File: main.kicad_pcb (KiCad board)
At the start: 2 copper layers, 19 parts, among them SW1 Switch, SW2 Switch, SW3 Switch, SW4 Switch, SW5 Switch, SW6 Switch, SW7 Switch, SW8 Switch, SW9 Switch

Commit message: finished PCB
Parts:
- moved A1 64.2 mm to (138.5, 45.0), turned to -90 degrees
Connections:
- net col 3 renamed Net-(A1-GPIO6)
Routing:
- net Net-(A1-GPIO6): track 113.5 -> 394.6 mm
- net col 1: track 54.9 -> 191.1 mm
- net row 2: track 142.4 -> 102.9 mm
- net Net-(A1-GPIO0): track 104.0 -> 75.8 mm
- net row 3: track 104.3 -> 128.1 mm
- net col2: track 56.3 -> 69.7 mm
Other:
- board outline added: 70.5 x 86 mm

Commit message: made shell for pcb
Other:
- board size 70.5 x 86 mm -> 80 x 88.5 mm
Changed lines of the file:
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@@
 	)
 	(gr_rect
-		(start 108 28)
-		(end 178.5 114)
+		(start 108 27)
+		(end 188 115.5)
 		(stroke
 			(width 0.05)
@@
 		(fill no)
 		(layer "Edge.Cuts")
+	)
+	(dimension
+		(type orthogonal)
+		(layer "Edge.Cuts")
+		(pts
+			(xy 108.5 28) (xy 108.5 114)
+		)
+		(height -25)
+		(orientation 1)
+		(format
+			(prefix "")
+			(suffix "")
+			(units 3)
+			(units_format 0)
+			(precision 4)
+			(suppress_zeroes yes)
+		)
+		(style
+			(thickness 0.05)
+			(arrow_length 1.27)
+			(text_position_mode 0)
+			(arrow_direction outward)
+			(extension_height 0.58642)
+			(extension_offset 0.5)
+			(keep_text_aligned yes)
+		)
+		(gr_text "86"
+			(at 82.35 71 90)
+			(layer "Edge.Cuts")
+			(effects
+				(font
+					(size 1 1)
+					(thickness 0.15)
+				)
+			)
+		)
+	)
+	(dimension
+		(type orthogonal)
+		(layer "Edge.Cuts")
+		(pts
+			(xy 178.5 114) (xy 109 114)
+		)
+		(height 21)
+		(orientation 0)
+		(format
+			(prefix "")
+			(suffix "")
+			(units 3)
+			(units_format 0)
+			(precision 4)
+			(suppress_zeroes yes)
+		)
+		(style
+			(thickness 0.05)
+			(arrow_length 1.27)
+			(text_position_mode 0)
+			(arrow_direction outward)
+			(extension_height 0.58642)
+			(extension_offset 0.5)
+			(keep_text_aligned yes)
+		)
+		(gr_text "69.5"
+			(at 143.75 133.85 0)
+			(layer "Edge.Cuts")
+			(effects
+				(font
+					(size 1 1)
+					(thickness 0.15)
+				)
+			)
+		)
 	)
 	(segment
@@
 			)
 		)
+	)
+	(zone
+		(net 0)
+		(net_name "")
+		(layer "User.1")
+		(hatch edge 0.5)
+		(connect_pads
+			(clearance 0)
+		)
+		(min_thickness 0.25)
+		(filled_areas_thickness no)
+		(keepout
+			(tracks not_allowed)
+			(vias not_allowed)
+			(pads not_allowed)
+			(copperpour allowed)
+			(footprints allowed)
+		)
+		(placement
+			(enabled no)
+			(sheetname "/")
+		)
+		(fill
+			(thermal_gap 0.5)
+			(thermal_bridge_width 0.5)
+		)
+		(polygon
+			(pts
+				(xy 192 24) (xy 192 118) (xy 105 118) (xy 104.5 117.5) (xy 104.5 24.5) (xy 105 24)
+			)
+		)

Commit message: fixed pcb
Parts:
- moved A1 2.89 mm to (138.5, 42.1), turned to 90 degrees
- moved D7 0.42 mm to (168.5, 67.5)
- moved D1 0.23 mm to (130.5, 67.5)
- moved D4 0.23 mm to (149.5, 67.5)
- moved SW7 0.10 mm to (160.0, 65.0)
- moved D3 0.08 mm to (130.5, 105.5)
- moved D6 0.08 mm to (149.5, 105.5)
- moved D9 0.08 mm to (168.5, 105.5)
- moved SW2 0.08 mm to (121.9, 84.1)
- moved SW5 0.08 mm to (140.9, 84.1)
- moved SW8 0.08 mm to (159.9, 84.1)
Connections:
- A1 pad 1: Net-(A1-GPIO0) -> unconnected-(A1-GPIO0-Pad1)
- A1 pad 10: unconnected-(A1-GPIO7-Pad10) -> Net-(A1-GPIO7)
- A1 pad 11: unconnected-(A1-GPIO8-Pad11) -> Net-(A1-GPIO8)
- A1 pad 2: row 2 -> unconnected-(A1-GPIO1-Pad2)
- A1 pad 4: row 3 -> Net-(A1-GPIO2)
- A1 pad 5: unconnected-(A1-GPIO3-Pad5) -> Net-(A1-GPIO3)
- A1 pad 6: col 1 -> Net-(A1-GPIO4)
- A1 pad 7: col 2 -> unconnected-(A1-GPIO5-Pad7)
- D1 pad 1: Net-(A1-GPIO0) -> Net-(A1-GPIO2)
- D2 pad 1: row 2 -> Net-(A1-GPIO3)
- D3 pad 1: row 3 -> Net-(A1-GPIO4)
- D4 pad 1: Net-(A1-GPIO0) -> Net-(A1-GPIO2)
- D5 pad 1: row 2 -> Net-(A1-GPIO3)
- D6 pad 1: row 3 -> Net-(A1-GPIO4)
- D7 pad 1: Net-(A1-GPIO0) -> Net-(A1-GPIO2)
- D8 pad 1: row 2 -> Net-(A1-GPIO3)
- D9 pad 1: row 3 -> Net-(A1-GPIO4)
- SW1 pad 1: col 1 -> Net-(A1-GPIO6)
- SW2 pad 1: col 1 -> Net-(A1-GPIO6)
- SW3 pad 1: col 1 -> Net-(A1-GPIO6)
- SW4 pad 1: col2 -> Net-(A1-GPIO7)
- SW5 pad 1: col2 -> Net-(A1-GPIO7)
- SW6 pad 1: col2 -> Net-(A1-GPIO7)
- SW7 pad 1: Net-(A1-GPIO6) -> Net-(A1-GPIO8)
- SW8 pad 1: Net-(A1-GPIO6) -> Net-(A1-GPIO8)
- SW9 pad 1: Net-(A1-GPIO6) -> Net-(A1-GPIO8)
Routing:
- net Net-(A1-GPIO6): track 394.6 -> 66.0 mm
- net col 1: track 191.1 -> 0.00 mm
- net Net-(A1-GPIO4): track 0.00 -> 138.3 mm
- net row 3: track 128.1 -> 0.00 mm
- net Net-(A1-GPIO3): track 0.00 -> 121.3 mm
- net Net-(A1-GPIO2): track 0.00 -> 105.0 mm
- net row 2: track 102.9 -> 0.00 mm
- net Net-(A1-GPIO0): track 75.8 -> 0.00 mm
- net col2: track 69.7 -> 0.00 mm
- net Net-(A1-GPIO8): track 0.00 -> 65.9 mm
- net Net-(A1-GPIO7): track 0.00 -> 49.5 mm
- removed copper zone on B.Cu, net (none)
- removed copper zone on F.Cu, net (none)
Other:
- board size 80 x 88.5 mm -> 61.8 x 85 mm

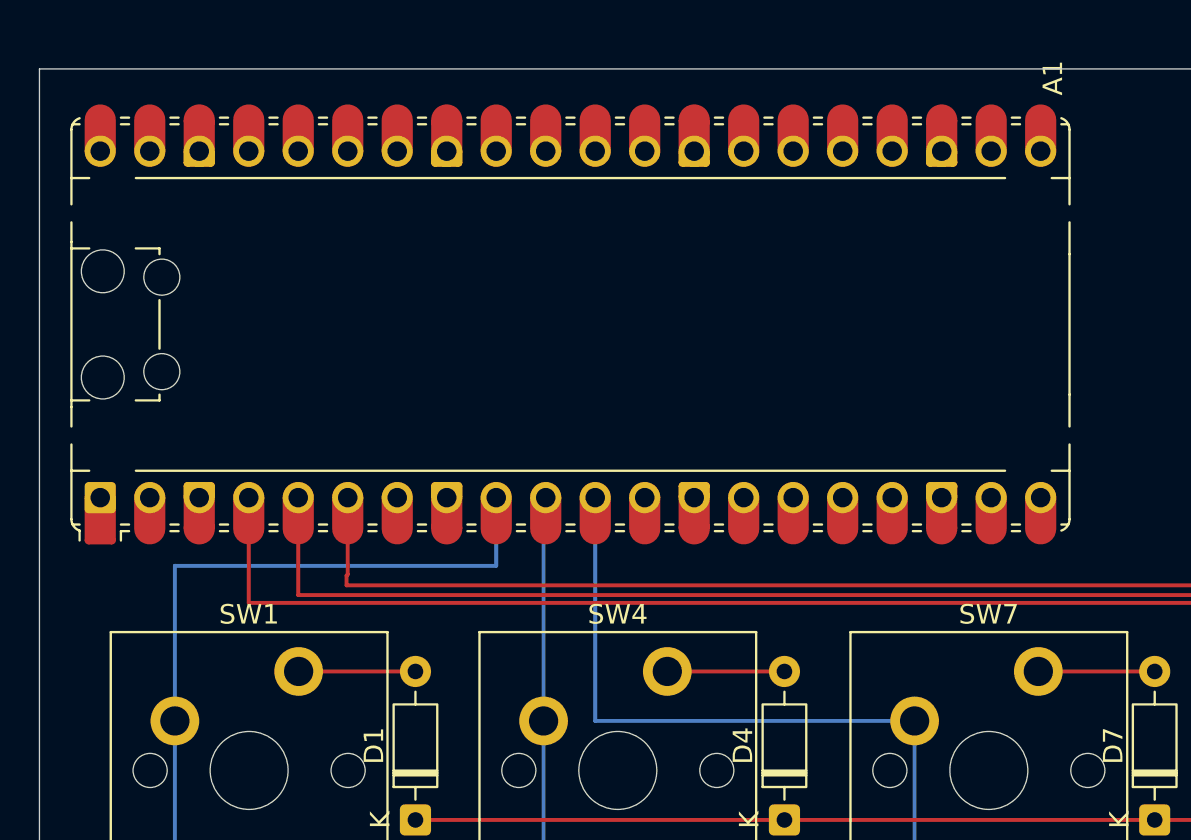
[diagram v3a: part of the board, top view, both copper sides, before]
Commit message: added new case model
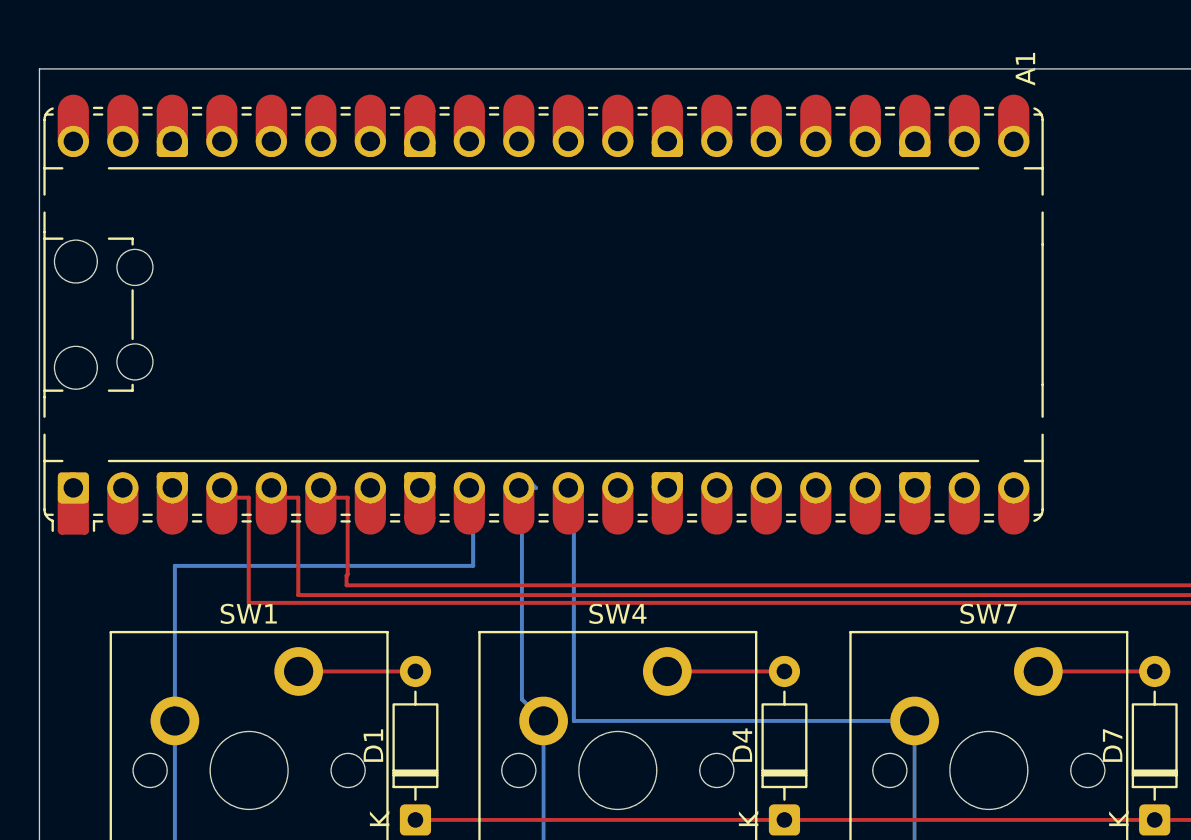
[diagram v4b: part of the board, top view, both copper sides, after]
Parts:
- moved A1 1.47 mm to (137.1, 41.6)
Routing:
- net Net-(A1-GPIO7): track 49.5 -> 52.5 mm
- net Net-(A1-GPIO8): track 65.9 -> 67.9 mm
- net Net-(A1-GPIO4): track 138.3 -> 139.9 mm
- net Net-(A1-GPIO3): track 121.3 -> 122.9 mm
- net Net-(A1-GPIO2): track 105.0 -> 106.6 mm
